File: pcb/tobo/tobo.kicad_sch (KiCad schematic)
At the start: 93 parts, among them J1 Molex 538-54548-2272, J2 Conn_01x02_Pin, J4 Molex 538-54548-2472, J5 Conn_01x09_Pin, J6 Conn_01x09_Pin, J7 Conn_01x09_Pin, J8 Hroparts Elec TYPE-C-31-M-12, U1 TS5A23167, U10 5015, U11 5015, U12 5015, U13 5015, U14 CH340E, U2 ATmega328P-A, U3 TS5A23167, U4 TS5A23167, U5 TS5A23167, U6 5015, U7 5015, U8 5015, U9 5015, X7 TestPoint, Y4 TestPoint

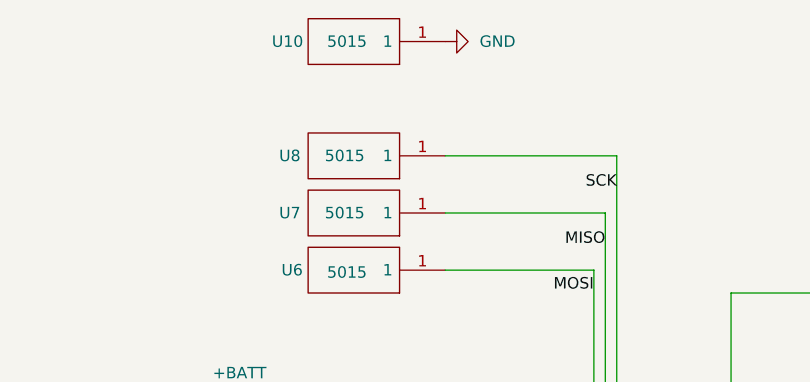
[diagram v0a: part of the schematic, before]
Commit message: Normalize PCB trace thickness and add a VCC attachment
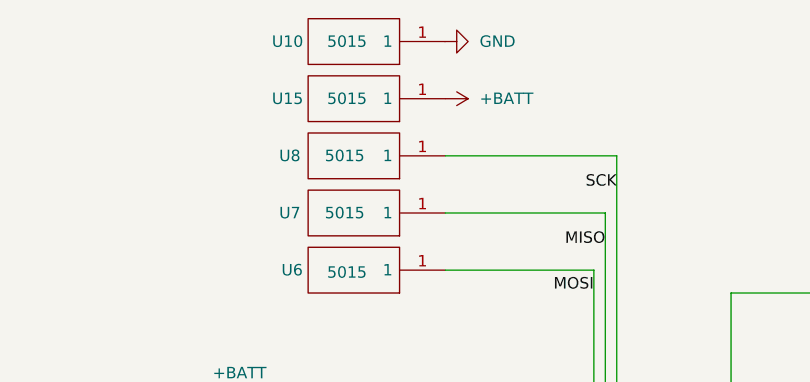
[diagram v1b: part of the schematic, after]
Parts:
- added U15: 5015, tobo-footprints:5015, symbol tobo-components:5015
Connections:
- net +BATT: now also U15.1
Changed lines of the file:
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@@
 	)
 	(symbol
+		(lib_id "power:+BATT")
+		(at 97.79 25.4 270)
+		(unit 1)
+		(exclude_from_sim no)
+		(in_bom yes)
+		(on_board yes)
+		(dnp no)
+		(fields_autoplaced yes)
+		(property "Reference" "#PWR027"
+			(at 93.98 25.4 0)
+			(effects
+				(font
+					(size 1.27 1.27)
+				)
+				(hide yes)
+			)
+		)
+		(property "Value" "+BATT"
+			(at 101.6 25.3999 90)
+			(effects
+				(font
+					(size 1.27 1.27)
+				)
+				(justify left)
+			)
+		)
+		(property "Footprint" ""
+			(at 97.79 25.4 0)
+			(effects
+				(font
+					(size 1.27 1.27)
+				)
+				(hide yes)
+			)
+		)
+		(property "Datasheet" ""
+			(at 97.79 25.4 0)
+			(effects
+				(font
+					(size 1.27 1.27)
+				)
+				(hide yes)
+			)
+		)
+		(property "Description" "Power symbol creates a global label with name \"+BATT\""
+			(at 97.79 25.4 0)
+			(effects
+				(font
+					(size 1.27 1.27)
+				)
+				(hide yes)
+			)
+		)
+		(pin "1"
+		)
+		(instances
+			(project "tobo"
+				(path "/ce2fc4a9-618f-4cc1-898a-224ffa79d770"
+					(reference "#PWR027")
+					(unit 1)
+				)
+			)
+		)
+	)
+	(symbol
 		(lib_id "power:GND")
 		(at 196.85 137.16 270)
@@
 					(unit 1)
 				)
+			)
+		)
+	)
+	(symbol
+		(lib_id "tobo-components:5015")
+		(at 97.79 25.4 180)
+		(unit 1)
+		(exclude_from_sim no)
+		(in_bom yes)
+		(on_board yes)
+		(dnp no)
+		(property "Reference" "U15"
+			(at 80.264 25.4 0)
+			(effects
+				(font
+					(size 1.27 1.27)
+				)
+			)
+		)
+		(property "Value" "5015"
+			(at 86.868 25.4 0)
+			(effects
+				(font
+					(size 1.27 1.27)
+				)
+			)
+		)
+		(property "Footprint" "tobo-footprints:5015"
+			(at 81.28 27.94 0)
+			(effects
+				(font
+					(size 1.27 1.27)
+				)
+				(justify left)
+				(hide yes)
+			)
+		)
+		(property "Datasheet" "http://www.keyelco.com/product-pdf.cfm?p=1353"
+			(at 81.28 25.4 0)
+			(effects
+				(font
+					(size 1.27 1.27)
+				)
+				(justify left)
+				(hide yes)
+			)
+		)
+		(property "Description" "Conn Test Point 1 POS Solder ST SMD 1 Port T/R"
+			(at 81.28 22.86 0)
+			(effects
+				(font
+					(size 1.27 1.27)
+				)
+				(justify left)
+				(hide yes)
+			)
+		)
+		(property "Height" "1.52"
+			(at 81.28 20.32 0)
+			(effects
+				(font
+					(size 1.27 1.27)
+				)
+				(justify left)
+				(hide yes)
+			)
+		)
+		(property "Manufacturer_Name" "Keystone Electronics"
+			(at 81.28 17.78 0)
+			(effects
+				(font
+					(size 1.27 1.27)
+				)
+				(justify left)
+				(hide yes)
+			)
+		)
+		(property "Manufacturer_Part_Number" "5015"
+			(at 81.28 15.24 0)
+			(effects
+				(font
+					(size 1.27 1.27)
+				)
+				(justify left)
+				(hide yes)
+			)
+		)
+		(property "Mouser Part Number" "534-5015"
+			(at 81.28 12.7 0)
+			(effects
+				(font
+					(size 1.27 1.27)
+				)
+				(justify left)
+				(hide yes)
+			)
+		)
+		(property "Mouser Price/Stock" "https://www.mouser.co.uk/ProductDetail/Keystone-Electronics/5015?qs=qOqV1E1P08ShW56PtUq2FA%3D%3D"
+			(at 81.28 10.16 0)
+			(effects
+				(font
+					(size 1.27 1.27)
+				)
+				(justify left)
+				(hide yes)
+			)
+		)
+		(property "Arrow Part Number" "5015"
+			(at 81.28 7.62 0)
+			(effects
+				(font
+					(size 1.27 1.27)
+				)
+				(justify left)
+				(hide yes)
+			)
+		)
+		(property "Arrow Price/Stock" "https://www.arrow.com/en/products/5015/keystone-electronics?utm_currency=USD&region=europe"
+			(at 81.28 5.08 0)
+			(effects
+				(font
+					(size 1.27 1.27)
+				)
+				(justify left)
+				(hide yes)
+			)
+		)
+		(pin "1"
+		)
+		(instances
+			(project "tobo"
+				(path "/ce2fc4a9-618f-4cc1-898a-224ffa79d770"
+					(reference "U15")
+					(unit 1)
+				)

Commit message: A pinmap, maybe
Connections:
- net BTN8 is gone; now on net BTN7: J5.8 (Pin_8), J6.8 (Pin_8), J7.8 (Pin_8), R18.2, U2.7 (XTAL1/PB6)
- net BTN1: now also J5.2 (Pin_2), J6.2 (Pin_2), J7.2 (Pin_2), R24.2, S2.2 (NO), U2.13 (PB1); no longer J5.1 (Pin_1), J6.1 (Pin_1), J7.1 (Pin_1), R25.2, S1.2 (NO), U2.14 (PB2)
- net BTN2: now also J5.3 (Pin_3), J6.3 (Pin_3), J7.3 (Pin_3), R23.2, S3.2 (NO), U2.12 (PB0); no longer J5.2 (Pin_2), J6.2 (Pin_2), J7.2 (Pin_2), R24.2, S2.2 (NO), U2.13 (PB1)
- net BTN3: now also J5.4 (Pin_4), J6.4 (Pin_4), J7.4 (Pin_4), R22.2, S4.2 (NO), U2.11 (PD7); no longer J5.3 (Pin_3), J6.3 (Pin_3), J7.3 (Pin_3), R23.2, S3.2 (NO), U2.12 (PB0)
- net BTN4: now also J5.5 (Pin_5), J6.5 (Pin_5), J7.5 (Pin_5), R21.2, S5.2 (NO), U2.10 (PD6); no longer J5.4 (Pin_4), J6.4 (Pin_4), J7.4 (Pin_4), R22.2, S4.2 (NO), U2.11 (PD7)
- net BTN5: now also J5.6 (Pin_6), J6.6 (Pin_6), J7.6 (Pin_6), R20.2, U2.9 (PD5); no longer J5.5 (Pin_5), J6.5 (Pin_5), J7.5 (Pin_5), R21.2, S5.2 (NO), U2.10 (PD6)
- net BTN6: now also J5.7 (Pin_7), J6.7 (Pin_7), J7.7 (Pin_7), R19.2, U2.8 (XTAL2/PB7); no longer J5.6 (Pin_6), J6.6 (Pin_6), J7.6 (Pin_6), R20.2, U2.9 (PD5)
- net BTN7: no longer J5.7 (Pin_7), J6.7 (Pin_7), J7.7 (Pin_7), R19.2, U2.8 (XTAL2/PB7)
- new net BTN0: J5.1 (Pin_1), J6.1 (Pin_1), J7.1 (Pin_1), R25.2, S1.2 (NO), U2.14 (PB2)
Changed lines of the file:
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@@
 		)
 	)
-	(label "BTN8"
+	(label "BTN7"
 		(at 102.87 186.69 0)
 		(fields_autoplaced yes)
@@
 		)
 	)
-	(label "BTN5"
+	(label "BTN4"
 		(at 95.25 194.31 0)
 		(fields_autoplaced yes)
@@
 		)
 	)
-	(label "BTN3"
+	(label "BTN2"
 		(at 104.14 179.07 0)
 		(fields_autoplaced yes)
@@
 		)
 	)
-	(label "BTN1"
+	(label "BTN0"
 		(at 99.06 184.15 0)
 		(fields_autoplaced yes)
@@
 		)
 	)
-	(label "BTN4"
+	(label "BTN3"
 		(at 92.71 196.85 0)
 		(fields_autoplaced yes)
@@
 		)
 	)
-	(label "BTN6"
+	(label "BTN5"
 		(at 97.79 191.77 0)
 		(fields_autoplaced yes)
@@
 		)
 	)
-	(label "BTN2"
+	(label "BTN1"
 		(at 101.6 181.61 0)
 		(fields_autoplaced yes)
@@
 		)
 	)
-	(label "BTN7"
+	(label "BTN6"
 		(at 100.33 189.23 0)
 		(fields_autoplaced yes)

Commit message: PCB tweaks
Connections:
- net ?,?: now reaches U2.1 (PD3), U5.7 (IN1)
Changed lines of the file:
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@@
 	(wire
 		(pts
-			(xy 91.44 133.35) (xy 90.17 133.35)
+			(xy 115.57 38.1) (xy 115.57 82.55)
 		)
 		(stroke
@@
 	(wire
 		(pts
-			(xy 115.57 38.1) (xy 115.57 82.55)
+			(xy 110.49 100.33) (xy 90.17 100.33)
 		)
 		(stroke
@@
 	(wire
 		(pts
-			(xy 110.49 100.33) (xy 90.17 100.33)
+			(xy 330.2 167.64) (xy 330.2 162.56)
 		)
 		(stroke
@@
 	(wire
 		(pts
-			(xy 330.2 167.64) (xy 330.2 162.56)
+			(xy 130.81 232.41) (xy 140.97 232.41)
 		)
 		(stroke
@@
 	(wire
 		(pts
-			(xy 130.81 232.41) (xy 140.97 232.41)
+			(xy 90.17 120.65) (xy 120.65 120.65)
 		)
 		(stroke
@@
 	(wire
 		(pts
-			(xy 90.17 120.65) (xy 120.65 120.65)
+			(xy 189.23 144.78) (xy 190.5 144.78)
 		)
 		(stroke
@@
 	(wire
 		(pts
-			(xy 189.23 144.78) (xy 190.5 144.78)
+			(xy 95.25 90.17) (xy 95.25 189.23)
 		)
 		(stroke
@@
 	(wire
 		(pts
-			(xy 99.06 74.93) (xy 99.06 181.61)
+			(xy 101.6 74.93) (xy 101.6 181.61)
 		)
 		(stroke
@@
 	(wire
 		(pts
-			(xy 90.17 128.27) (xy 93.98 128.27)
+			(xy 90.17 128.27) (xy 92.71 128.27)
 		)
 		(stroke
@@
 	(wire
 		(pts
-			(xy 91.44 133.35) (xy 91.44 196.85)
+			(xy 90.17 133.35) (xy 90.17 196.85)
 		)
 		(stroke
@@
 	(wire
 		(pts
-			(xy 90.17 74.93) (xy 99.06 74.93)
+			(xy 90.17 74.93) (xy 101.6 74.93)
 		)
 		(stroke
@@
 	(wire
 		(pts
-			(xy 99.06 181.61) (xy 116.84 181.61)
+			(xy 101.6 181.61) (xy 116.84 181.61)
 		)
 		(stroke
@@
 	(wire
 		(pts
-			(xy 91.44 196.85) (xy 132.08 196.85)
+			(xy 90.17 196.85) (xy 132.08 196.85)
 		)
 		(stroke
@@
 	(wire
 		(pts
-			(xy 90.17 72.39) (xy 100.33 72.39)
+			(xy 90.17 72.39) (xy 102.87 72.39)
 		)
 		(stroke
@@
 	(wire
 		(pts
-			(xy 90.17 130.81) (xy 92.71 130.81)
+			(xy 90.17 130.81) (xy 91.44 130.81)
 		)
 		(stroke
@@
 	(wire
 		(pts
-			(xy 93.98 128.27) (xy 93.98 191.77)
+			(xy 92.71 128.27) (xy 92.71 191.77)
 		)
 		(stroke
@@
 	(wire
 		(pts
-			(xy 90.17 77.47) (xy 97.79 77.47)
+			(xy 90.17 77.47) (xy 100.33 77.47)
 		)
 		(stroke
@@
 	(wire
 		(pts
-			(xy 95.25 90.17) (xy 95.25 189.23)
-		)
-		(stroke
-			(width 0)
-			(type default)
-		)
-	)
-	(wire
-		(pts
 			(xy 328.93 213.36) (xy 331.47 213.36)
 		)
@@
 	(wire
 		(pts
-			(xy 96.52 87.63) (xy 96.52 186.69)
-		)
-		(stroke
-			(width 0)
-			(type default)
-		)
-	)
-	(wire
-		(pts
 			(xy 124.46 180.34) (xy 144.78 180.34)
 		)
@@
 	(wire
 		(pts
-			(xy 92.71 194.31) (xy 129.54 194.31)
+			(xy 91.44 194.31) (xy 129.54 194.31)
 		)
 		(stroke
@@
 	(wire
 		(pts
+			(xy 90.17 90.17) (xy 95.25 90.17)
+		)
+		(stroke
+			(width 0)
+			(type default)
+		)
+	)
+	(wire
+		(pts
 			(xy 127 177.8) (xy 144.78 177.8)
 		)
@@
 	(wire
 		(pts
-			(xy 97.79 184.15) (xy 119.38 184.15)
+			(xy 100.33 184.15) (xy 119.38 184.15)
 		)
 		(stroke
@@
 	(wire
 		(pts
-			(xy 92.71 130.81) (xy 92.71 194.31)
+			(xy 91.44 130.81) (xy 91.44 194.31)
 		)
 		(stroke
@@
 	(wire
 		(pts
-			(xy 96.52 186.69) (xy 121.92 186.69)
+			(xy 97.79 186.69) (xy 121.92 186.69)
 		)
 		(stroke
@@
 	(wire
 		(pts
-			(xy 90.17 87.63) (xy 96.52 87.63)
+			(xy 90.17 87.63) (xy 97.79 87.63)
 		)
 		(stroke
@@
 	(wire
 		(pts
-			(xy 90.17 90.17) (xy 95.25 90.17)
-		)
-		(stroke
-			(width 0)
-			(type default)
-		)
-	)
-	(wire
-		(pts
 			(xy 85.09 228.6) (xy 91.44 228.6)
 		)
@@
 	(wire
 		(pts
-			(xy 100.33 179.07) (xy 114.3 179.07)
+			(xy 102.87 179.07) (xy 114.3 179.07)
 		)
 		(stroke
@@
 	(wire
 		(pts
+			(xy 97.79 87.63) (xy 97.79 186.69)
+		)
+		(stroke
+			(width 0)
+			(type default)
+		)
+	)
+	(wire
+		(pts
 			(xy 210.82 154.94) (xy 209.55 154.94)
 		)
@@
 	(wire
 		(pts
-			(xy 97.79 77.47) (xy 97.79 184.15)
+			(xy 100.33 77.47) (xy 100.33 184.15)
 		)
 		(stroke
@@
 	(wire
 		(pts
-			(xy 93.98 191.77) (xy 127 191.77)
+			(xy 92.71 191.77) (xy 127 191.77)
 		)
 		(stroke
@@
 	(wire
 		(pts
-			(xy 100.33 72.39) (xy 100.33 179.07)
+			(xy 102.87 72.39) (xy 102.87 179.07)
 		)
 		(stroke
@@
 	)
 	(label "BTN0"
-		(at 99.06 184.15 0)
+		(at 100.33 184.15 0)
 		(fields_autoplaced yes)
 		(effects
@@
 		)
 	)
+	(label "7,6"
+		(at 151.13 132.08 0)
+		(fields_autoplaced yes)
+		(effects
+			(font
+				(size 1.27 1.27)
+			)
+			(justify left bottom)
+		)
+	)
 	(label "6,4"
 		(at 175.26 68.58 0)
@@
 		)
 	)
+	(label "7,5"
+		(at 152.4 105.41 0)
+		(fields_autoplaced yes)
+		(effects
+			(font
+				(size 1.27 1.27)
+			)
+			(justify left bottom)
+		)
+	)
 	(label "8,4"
 		(at 137.16 78.74 90)
@@
 		)
 	)
+	(label "?,?"
+		(at 151.13 123.19 0)
+		(fields_autoplaced yes)
+		(effects
+			(font
+				(size 1.27 1.27)
+			)
+			(justify left bottom)
+		)
+	)
 	(label "X7"
 		(at 232.41 77.47 0)
@@
 		(fields_autoplaced yes)
 		(effects
+			(font
+				(size 1.27 1.27)
+			)
+			(justify left bottom)
+		)
+	)
+	(label "7,7"
+		(at 147.32 111.76 0)
+		(fields_autoplaced yes)
+		(effects
